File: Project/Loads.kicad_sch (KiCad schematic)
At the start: 40 parts, among them IC1 DRDC3105F-7, IC10 DRDC3105F-7, IC11 DRDC3105F-7, IC12 DRDC3105F-7, IC13 DRDC3105F-7, IC14 DRDC3105F-7, IC15 DRDC3105F-7, IC16 DRDC3105F-7, IC17 DRDC3105F-7, IC2 DRDC3105F-7, IC4 DRDC3105F-7, IC5 DRDC3105F-7, IC6 DRDC3105F-7, IC7 DRDC3105F-7, IC8 DRDC3105F-7, IC9 DRDC3105F-7, J1 Conn_01x03_Socket, J2 Conn_01x03_Socket, J3 Conn_01x03_Socket, J4 Conn_01x03_Socket, J5 Conn_01x03_Socket, J6 Conn_01x03_Socket, J7 Conn_01x03_Socket, J8 Conn_01x03_Socket, K1 V23079C1103B301, K10 IMC03TS, K11 V23079C1103B301, K12 IMC03TS, K13 V23079C1103B301, K14 IMC03TS, K15 V23079C1103B301, K16 IMC03TS, K2 IMC03TS, K3 V23079C1103B301, K4 IMC03TS, K5 V23079C1103B301, K6 IMC03TS, K7 V23079C1103B301, K8 IMC03TS, K9 V23079C1103B301

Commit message: new schematic
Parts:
- IC1, IC10, IC11, IC12, IC13, IC14, IC15, IC16, IC17, IC2, IC4, IC5, IC6, IC7, IC8, IC9: footprint SOT96P240X110-3N -> Library:SOT96P240X110-3N
- J1: value Conn_01x03_Socket -> Load 0
- J2: value Conn_01x03_Socket -> Load 1
- J3: value Conn_01x03_Socket -> Load 2
- J4: value Conn_01x03_Socket -> Load 3
- J5: value Conn_01x03_Socket -> Load 4
- J6: value Conn_01x03_Socket -> Load 7
- J7: value Conn_01x03_Socket -> Load 6
- J8: value Conn_01x03_Socket -> Load 5
- K1, K11, K13, K15, K3, K5, K7, K9: footprint V23079A1001B301 -> Library:V23079A1001B301
- K10, K12, K14, K16, K2, K4, K6, K8: footprint IMC03TS -> Library:IMC03TS
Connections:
- net Ra_0: no longer K15.9 (COM_2)
- net Ra_7: now also K15.9 (COM_2)
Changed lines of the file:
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@@
 		)
 	)
-	(label "Ra_0"
+	(label "Ra_7"
 		(at 265.43 124.46 0)
 		(fields_autoplaced yes)
@@
 			)
 		)
-		(property "Footprint" "SOT96P240X110-3N"
+		(property "Footprint" "Library:SOT96P240X110-3N"
 			(at 58.42 207.95 0)
 			(effects
@@
 			)
 		)
-		(property "Footprint" "V23079A1001B301"
+		(property "Footprint" "Library:V23079A1001B301"
 			(at 115.57 171.12 0)
 			(effects
@@
 			)
 		)
-		(property "Footprint" "V23079A1001B301"
+		(property "Footprint" "Library:V23079A1001B301"
 			(at 118.11 280.34 0)
 			(effects
@@
 			)
 		)
-		(property "Footprint" "V23079A1001B301"
+		(property "Footprint" "Library:V23079A1001B301"
 			(at 255.27 214.3 0)
 			(effects
@@
 			)
 		)
-		(property "Footprint" "SOT96P240X110-3N"
+		(property "Footprint" "Library:SOT96P240X110-3N"
 			(at 196.85 158.42 0)
 			(effects
@@
 			)
 		)
-		(property "Footprint" "SOT96P240X110-3N"
+		(property "Footprint" "Library:SOT96P240X110-3N"
 			(at 198.12 214.3 0)
 			(effects
@@
 			)
 		)
-		(property "Value" "Conn_01x03_Socket"
+		(property "Value" "Load 6"
 			(at 252.222 72.644 0)
 			(effects
@@
 			)
 		)
-		(property "Value" "Conn_01x03_Socket"
+		(property "Value" "Load 2"
 			(at 112.522 105.664 0)
 			(effects
@@
 			)
 		)
-		(property "Footprint" "IMC03TS"
+		(property "Footprint" "Library:IMC03TS"
 			(at 96.52 115.24 0)
 			(effects
@@
 			)
 		)
-		(property "Footprint" "V23079A1001B301"
+		(property "Footprint" "Library:V23079A1001B301"
 			(at 115.57 243.51 0)
 			(effects
@@
 			)
 		)
-		(property "Footprint" "IMC03TS"
+		(property "Footprint" "Library:IMC03TS"
 			(at 96.52 154.61 0)
 			(effects
@@
 			)
 		)
-		(property "Footprint" "SOT96P240X110-3N"
+		(property "Footprint" "Library:SOT96P240X110-3N"
 			(at 58.42 131.75 0)
 			(effects
@@
 			)
 		)
-		(property "Value" "Conn_01x03_Socket"
+		(property "Value" "Load 4"
 			(at 115.062 178.054 0)
 			(effects
@@
 			)
 		)
-		(property "Footprint" "SOT96P240X110-3N"
+		(property "Footprint" "Library:SOT96P240X110-3N"
 			(at 196.85 197.79 0)
 			(effects
@@
 			)
 		)
-		(property "Footprint" "SOT96P240X110-3N"
+		(property "Footprint" "Library:SOT96P240X110-3N"
 			(at 57.15 227 0)
 			(effects
@@
 			)
 		)
-		(property "Footprint" "V23079A1001B301"
+		(property "Footprint" "Library:V23079A1001B301"
 			(at 257.81 134.29 0)
 			(effects
@@
 			)
 		)
-		(property "Footprint" "SOT96P240X110-3N"
+		(property "Footprint" "Library:SOT96P240X110-3N"
 			(at 198.12 174.93 0)
 			(effects
@@
 			)
 		)
-		(property "Footprint" "SOT96P240X110-3N"
+		(property "Footprint" "Library:SOT96P240X110-3N"
 			(at 60.96 280.34 0)
 			(effects
@@
 			)
 		)
-		(property "Footprint" "SOT96P240X110-3N"
+		(property "Footprint" "Library:SOT96P240X110-3N"
 			(at 200.66 134.29 0)
 			(effects
@@
 			)
 		)
-		(property "Footprint" "IMC03TS"
+		(property "Footprint" "Library:IMC03TS"
 			(at 96.52 191.44 0)
 			(effects
@@
 			)
 		)
-		(property "Footprint" "V23079A1001B301"
+		(property "Footprint" "Library:V23079A1001B301"
 			(at 255.27 174.93 0)
 			(effects
@@
 			)
 		)
-		(property "Footprint" "SOT96P240X110-3N"
+		(property "Footprint" "Library:SOT96P240X110-3N"
 			(at 58.42 171.12 0)
 			(effects
@@
 			)
 		)
-		(property "Value" "Conn_01x03_Socket"
+		(property "Value" "Load 7"
 			(at 252.222 112.014 0)
 			(effects
@@
 			)
 		)
-		(property "Footprint" "V23079A1001B301"
+		(property "Footprint" "Library:V23079A1001B301"
 			(at 115.57 207.95 0)
 			(effects
@@
 			)
 		)
-		(property "Footprint" "IMC03TS"
+		(property "Footprint" "Library:IMC03TS"
 			(at 96.52 227 0)
 			(effects
@@
 			)
 		)
-		(property "Footprint" "IMC03TS"
+		(property "Footprint" "Library:IMC03TS"
 			(at 238.76 117.78 0)
 			(effects
@@
 			)
 		)
-		(property "Footprint" "IMC03TS"
+		(property "Footprint" "Library:IMC03TS"
 			(at 99.06 263.83 0)
 			(effects
@@
 			)
 		)
-		(property "Value" "Conn_01x03_Socket"
+		(property "Value" "Load 5"
 			(at 254.762 32.004 0)
 			(effects
@@
 			)
 		)
-		(property "Footprint" "SOT96P240X110-3N"
+		(property "Footprint" "Library:SOT96P240X110-3N"
 			(at 58.42 243.51 0)
 			(effects
@@
 			)
 		)
-		(property "Footprint" "SOT96P240X110-3N"
+		(property "Footprint" "Library:SOT96P240X110-3N"
 			(at 199.39 117.78 0)
 			(effects
@@
 			)
 		)
-		(property "Footprint" "IMC03TS"
+		(property "Footprint" "Library:IMC03TS"
 			(at 236.22 158.42 0)
 			(effects
@@
 			)
 		)
-		(property "Footprint" "IMC03TS"
+		(property "Footprint" "Library:IMC03TS"
 			(at 236.22 197.79 0)
 			(effects
@@
 			)
 		)
-		(property "Footprint" "SOT96P240X110-3N"
+		(property "Footprint" "Library:SOT96P240X110-3N"
 			(at 57.15 191.44 0)
 			(effects
@@
 			)
 		)
-		(property "Value" "Conn_01x03_Socket"
+		(property "Value" "Load 0"
 			(at 112.522 29.464 0)
 			(effects
@@
 			)
 		)
-		(property "Footprint" "SOT96P240X110-3N"
+		(property "Footprint" "Library:SOT96P240X110-3N"
 			(at 57.15 115.24 0)
 			(effects
@@
 			)
 		)
-		(property "Footprint" "V23079A1001B301"
+		(property "Footprint" "Library:V23079A1001B301"
 			(at 115.57 131.75 0)
 			(effects
@@
 			)
 		)
-		(property "Value" "Conn_01x03_Socket"
+		(property "Value" "Load 3"
 			(at 112.522 141.224 0)
 			(effects
@@
 			)
 		)
-		(property "Footprint" "SOT96P240X110-3N"
+		(property "Footprint" "Library:SOT96P240X110-3N"
 			(at 59.69 263.83 0)
 			(effects
@@
 			)
 		)
-		(property "Footprint" "SOT96P240X110-3N"
+		(property "Footprint" "Library:SOT96P240X110-3N"
 			(at 57.15 154.61 0)
 			(effects
@@
 			)
 		)
-		(property "Value" "Conn_01x03_Socket"
+		(property "Value" "Load 1"
 			(at 112.522 68.834 0)
 			(effects

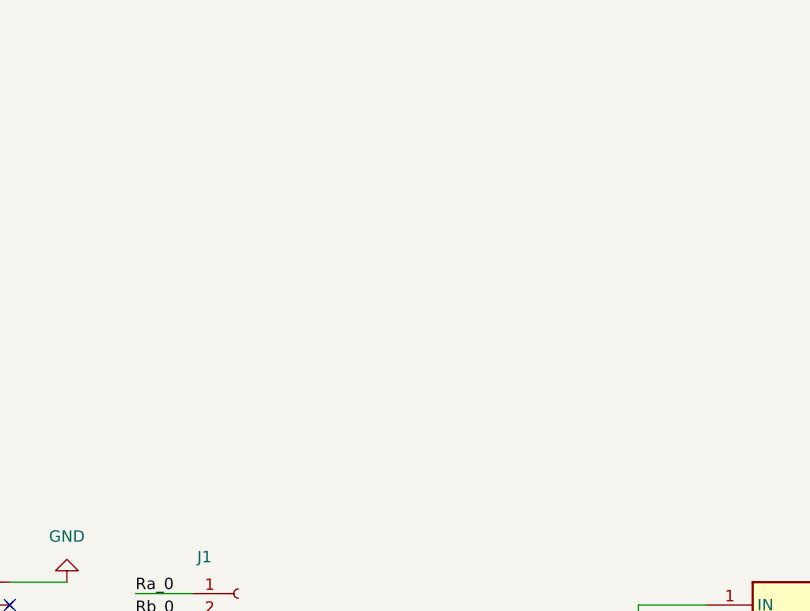
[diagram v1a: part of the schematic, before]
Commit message: update schematic
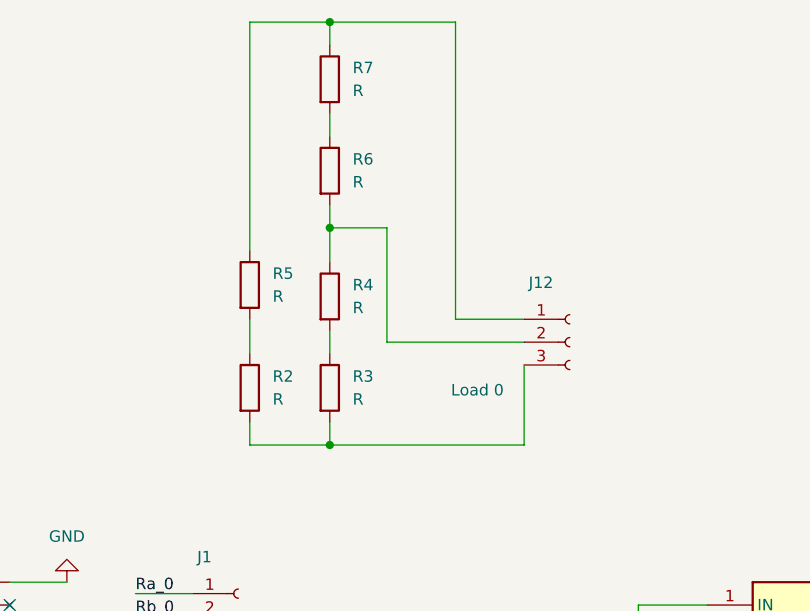
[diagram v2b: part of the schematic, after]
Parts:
- added J12: Load 0, Connector_PinHeader_2.54mm:PinHeader_1x03_P2.54mm_Horizontal, symbol Connector:Conn_01x03_Socket
- added R2, R3, R4, R6, R7: R, Resistor_SMD:R_0805_2012Metric, symbol Device:R
- added R5: R, Resistor_THT:R_Axial_DIN0614_L14.3mm_D5.7mm_P20.32mm_Horizontal, symbol Device:R
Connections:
- new net: J12.1 (Pin_1), R5.1, R7.1
- new net: J12.2 (Pin_2), R4.1, R6.2
- new net: J12.3 (Pin_3), R2.2, R3.2
- new net: R2.1, R5.2
- new net: R3.1, R4.2
- new net: R6.1, R7.2
